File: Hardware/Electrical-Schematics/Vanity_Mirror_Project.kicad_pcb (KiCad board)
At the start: 2 copper layers, 61 x 40.6 mm, 42 parts, among them IC1 SN74LV1T34QDBVRQ1, IC2 FDC1004QDGSRQ1, J1 USB_C_Receptacle_USB2.0_14P, Q1 2N7002, Q2 2N7002, SW1 RST, U1 CH340C, U2 ESP-12F, U3 USBLC6-2SC6, U4 XL1509-3.3

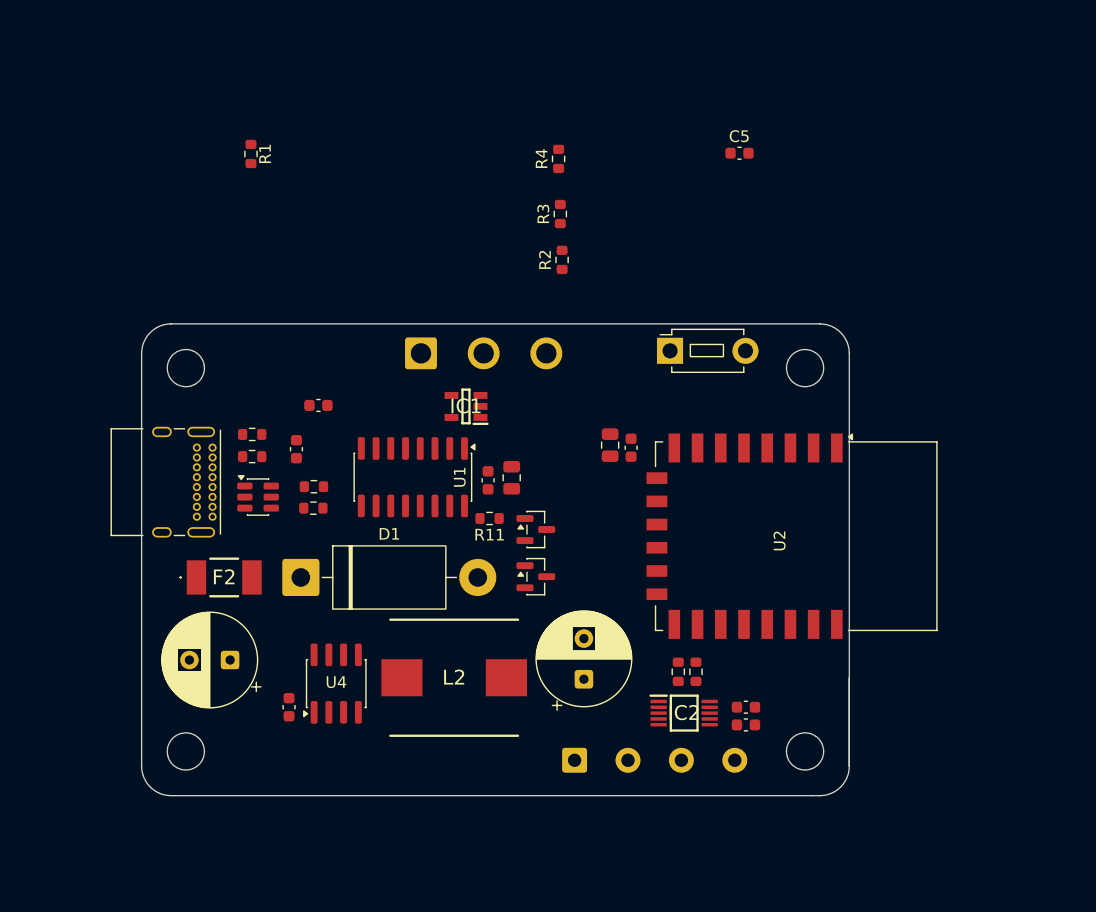
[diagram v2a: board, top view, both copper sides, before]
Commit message: 1st PCB design
Finished the routing of the PCB and added BJTs for auto programming and auto resetting.
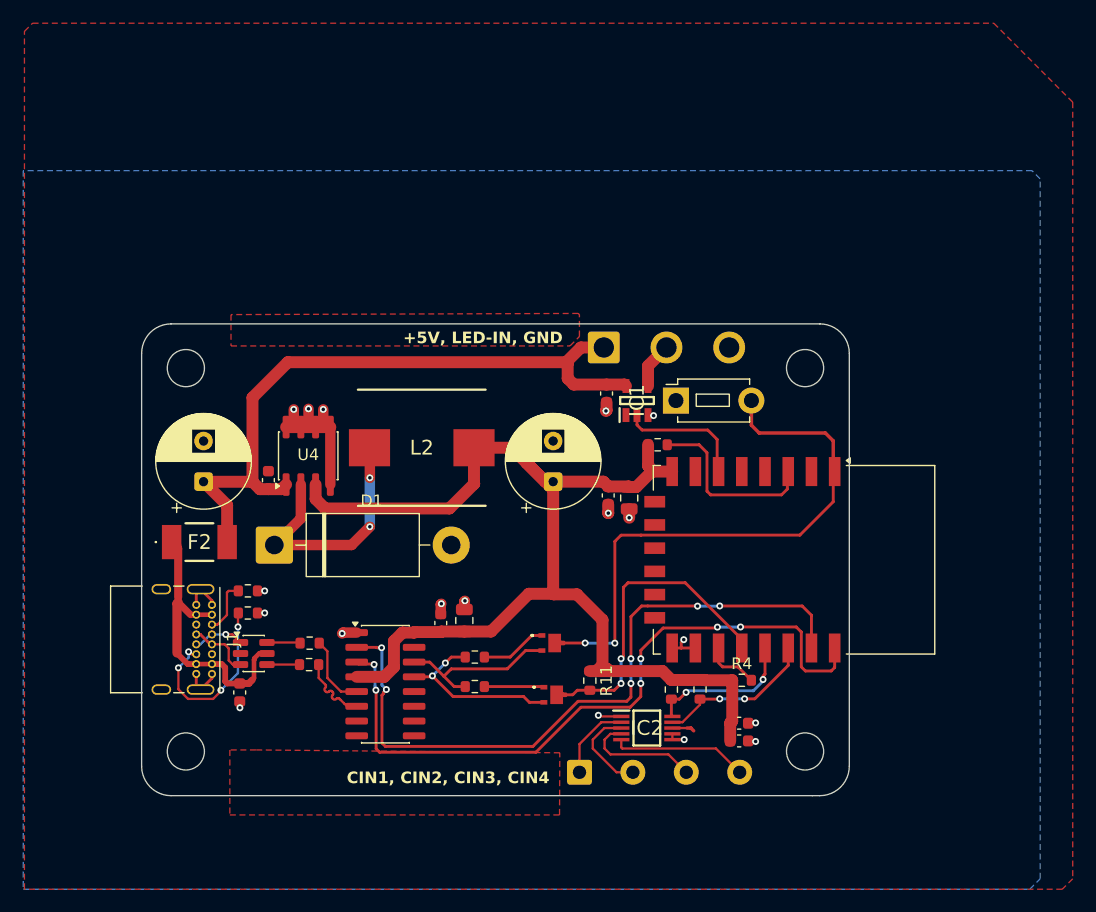
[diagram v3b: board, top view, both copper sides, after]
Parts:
- removed C5: 0.1uF, Capacitor_SMD:C_0603_1608Metric
- Q1, Q2: value 2N7002 -> Q_NPN_BEC; footprint Package_TO_SOT_SMD:SOT-23 -> VanityMirror_FootPrints:PMEG2020EPASX
- R11: value 220 -> 10k
- R2, R3: value 10k -> 12k
- moved R4 47.6 mm to (153.3, 132.3), turned to 0 degrees
- moved R1 43.1 mm to (146.1, 112.0), turned to 180 degrees
- moved R3 41.4 mm to (130.3, 132.8), turned to 180 degrees
- moved R2 35.0 mm to (130.3, 130.3), turned to 180 degrees
- moved C8 24.8 mm to (141.7, 107.6), turned to -90 degrees
- moved C4 21.5 mm to (110.0, 133.3), turned to -90 degrees
- moved L2 20.0 mm to (125.7, 112.3)
- moved U4 19.8 mm to (116.0, 113.0)
- moved C11 19.6 mm to (112.5, 115.1)
- moved U1 18.0 mm to (122.6, 132.6), turned to 0 degrees
- moved C10 17.2 mm to (137.1, 115.2)
- moved R11 16.4 mm to (140.2, 132.3), turned to -90 degrees
- moved LED_Pins1 15.8 mm to (141.4, 103.6)
- moved C12 15.5 mm to (106.9, 115.2), turned to 90 degrees
- moved IC1 14.7 mm to (144.3, 108.2), turned to 90 degrees
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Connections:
- net Net-(U1-UD+) renamed /D+
- net Net-(U1-UD-) renamed /D-
- Q1 pad 1: /~{DTR} -> Net-(Q1-B)
- Q1 pad 2: GND -> Net-(Q1-E)
- Q1 pad 3: Net-(Q1-D) -> /~{RST}
- Q2 pad 1: Net-(Q2-G) -> Net-(Q2-B)
- Q2 pad 2: GND -> Net-(Q2-E)
- Q2 pad 3: Net-(Q2-D) -> /GPIO0
- R11 pad 1: Net-(Q2-G) -> +3.3V
- R11 pad 2: /~{RTS} -> /GPIO0
- R2 pad 1: Net-(Q2-D) -> Net-(Q1-B)
- R2 pad 2: +3.3V -> Net-(Q2-E)
- R3 pad 1: Net-(Q1-D) -> Net-(Q2-B)
- R3 pad 2: +3.3V -> Net-(Q1-E)
- SW1 pad 2: Net-(Q2-D) -> /~{RST}
- U1 pad 13: /~{DTR} -> Net-(Q2-E)
- U1 pad 14: /~{RTS} -> Net-(Q1-E)
- U2 pad 1: Net-(Q2-D) -> /~{RST}
- U2 pad 18: Net-(Q1-D) -> /GPIO0
- U2 pad 19: /SN74_1A -> /SDA
- U2 pad 6: /SDA -> /SN74_1A
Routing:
- net +3.3V: track 0.00 -> 105.2 mm
- net /TX: track 0.00 -> 60.7 mm, vias 0 -> 6
- net /RX: track 0.00 -> 60.1 mm, vias 0 -> 6
- net +5V: track 0.00 -> 59.6 mm
- net /~{RST}: track 0.00 -> 49.2 mm, vias 0 -> 2
- net GND: track 0.00 -> 35.4 mm, vias 0 -> 18
- net /GPIO0: track 0.00 -> 27.4 mm, vias 0 -> 2
- net Net-(U3-VBUS): track 0.00 -> 24.8 mm
- net Net-(D1-K): track 0.00 -> 21.9 mm, vias 0 -> 2
- net Net-(J1-CC2): track 0.00 -> 16.0 mm, vias 0 -> 4
- net Net-(U2-EN): track 0.00 -> 15.8 mm
- net Net-(Q2-E): track 0.00 -> 15.7 mm, vias 0 -> 2
- net Net-(Q1-E): track 0.00 -> 14.6 mm
- net /SCL: track 0.00 -> 13.8 mm, vias 0 -> 2
- net /SDA: track 0.00 -> 13.1 mm, vias 0 -> 2
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- added copper zone on B.Cu, net GND
- added copper zone on F.Cu, net GND
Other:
- outline, holes or cut-outs redrawn
- board text added: "+5V, LED-IN, GND"
- board text added: "CIN1, CIN2, CIN3, CIN4"

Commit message: updating the version
changing laptops so pushing the minor changes made so that the new laptop has the most recent version
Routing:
- net +3.3V: track 105.2 -> 109.1 mm
- net GND: vias 18 -> 22
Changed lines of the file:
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@@
+	)
+	(via
+		(at 146.05 133.223)
+		(size 0.6)
+		(drill 0.3)
+		(layers "F.Cu" "B.Cu")
+		(free yes)
+		(net 1)
 	)
 	(via
@@
 	)
 	(via
+		(at 145.288 133.223)
+		(size 0.6)
+		(drill 0.3)
+		(layers "F.Cu" "B.Cu")
+		(free yes)
+		(net 1)
+	)
+	(via
 		(at 129.4495 125.454)
 		(size 0.6)
@@
 		(drill 0.3)
 		(layers "F.Cu" "B.Cu")
+		(net 1)
+	)
+	(via
+		(at 146.05 133.985)
+		(size 0.6)
+		(drill 0.3)
+		(layers "F.Cu" "B.Cu")
+		(free yes)
+		(net 1)
+	)
+	(via
+		(at 145.288 133.985)
+		(size 0.6)
+		(drill 0.3)
+		(layers "F.Cu" "B.Cu")
+		(free yes)
 		(net 1)
 	)
@@
 	)
 	(segment
+		(start 152.475 134.874)
+		(end 152.475 135.825)
+		(width 1.03)
+		(layer "F.Cu")
+		(net 2)
+	)
+	(segment
 		(start 136.374251 115.190651)
 		(end 137.05 115.190651)
@@
 	)
 	(segment
+		(start 152.221 135.128)
+		(end 152.475 134.874)
+		(width 1.03)
+		(layer "F.Cu")
+		(net 2)
+	)
+	(segment
 		(start 145.63 114.32)
 		(end 147.3 114.32)
@@
 	)
 	(segment
+		(start 148.914 136.414)
+		(end 149.336 136.414)
+		(width 1.03)
+		(layer "F.Cu")
+		(net 2)
+	)
+	(segment
 		(start 137.05 115.190651)
 		(end 141.379651 115.190651)
@@
 	)
 	(segment
+		(start 148.914 136.414)
+		(end 148.586 136.414)
+		(width 0.5)
+		(layer "F.Cu")
+		(net 2)
+	)
+	(segment
 		(start 146.469 131.509)
 		(end 147.234 132.274)
@@
 	)
 	(segment
-		(start 148.914 136.414)
-		(end 149.152 136.652)
-		(width 0.3)
-		(layer "F.Cu")
-		(net 2)
-	)
-	(segment
 		(start 125.1225 128.145)
 		(end 125.075 128.1925)
@@
 	(segment
 		(start 152.475 132.3)
-		(end 152.475 135.825)
+		(end 152.475 134.874)
 		(width 1.03)
 		(layer "F.Cu")
@@
 	)
 	(segment
-		(start 148.586 136.414)
-		(end 148.914 136.414)
-		(width 0.3)
-		(layer "F.Cu")
-		(net 2)
-	)
-	(segment
 		(start 152.3 136)
 		(end 152.3 137.524)
@@
 		(start 141.794 115.605)
 		(end 143.555 115.605)
+		(width 1.03)
+		(layer "F.Cu")
+		(net 2)
+	)
+	(segment
+		(start 150.622 135.128)
+		(end 152.221 135.128)
+		(width 1.03)
+		(layer "F.Cu")
+		(net 2)
+	)
+	(segment
+		(start 149.336 136.414)
+		(end 150.622 135.128)
 		(width 1.03)
 		(layer "F.Cu")
@@
 	)
 	(segment
+		(start 146.875 112.014)
+		(end 149.62 112.014)
+		(width 0.25)
+		(layer "F.Cu")
+		(net 48)
+	)
+	(segment
+		(start 156.591 116.459)
+		(end 157.226 115.824)
+		(width 0.25)
+		(layer "F.Cu")
+		(net 48)
+	)
+	(segment
+		(start 149.62 112.014)
+		(end 150.3 112.694)
+		(width 0.25)
+		(layer "F.Cu")
+		(net 48)
+	)
+	(segment
+		(start 157.226 115.824)
+		(end 157.226 114.37)
+		(width 0.25)
+		(layer "F.Cu")
+		(net 48)
+	)
+	(segment
+		(start 150.3 116.01)
+		(end 150.749 116.459)
+		(width 0.25)
+		(layer "F.Cu")
+		(net 48)
+	)
+	(segment
 		(start 157.226 114.37)
 		(end 157.176 114.32)
@@
 	)
 	(segment
-		(start 150.3 116.01)
-		(end 150.622 116.332)
-		(width 0.25)
-		(layer "F.Cu")
-		(net 48)
-	)
-	(segment
-		(start 156.718 116.332)
-		(end 157.226 115.824)
-		(width 0.25)
-		(layer "F.Cu")
-		(net 48)
-	)
-	(segment
 		(start 150.3 112.694)
 		(end 150.3 116.01)
@@
 	)
 	(segment
-		(start 146.875 112.014)
-		(end 149.62 112.014)
-		(width 0.25)
-		(layer "F.Cu")
-		(net 48)
-	)
-	(segment
-		(start 150.622 116.332)
-		(end 156.718 116.332)
-		(width 0.25)
-		(layer "F.Cu")
-		(net 48)
-	)
-	(segment
-		(start 157.226 115.824)
-		(end 157.226 114.37)
-		(width 0.25)
-		(layer "F.Cu")
-		(net 48)
-	)
-	(segment
-		(start 149.62 112.014)
-		(end 150.3 112.694)
+		(start 150.749 116.459)
+		(end 156.591 116.459)
 		(width 0.25)
 		(layer "F.Cu")
@@
 		(priority 1)
 		(connect_pads
-			(clearance 0.3)
+			(clearance 0.6)
 		)
 		(min_thickness 0.25)
@@
 		(polygon
 			(pts
-				(xy 181.806449 82.5) (xy 181.806449 149.4) (xy 180.906449 150.3) (xy 91.506449 150.3) (xy 91.506449 76.4)
-				(xy 92.206449 75.7) (xy 175.006449 75.7)
+				(xy 187.833 83.312) (xy 187.833 156.337) (xy 187.579 156.591) (xy 88.138 156.591) (xy 88.138 82.677)
+				(xy 187.198 82.677)
 			)
 		)
 		(polygon
 			(pts
-				(xy 109.2 143.9) (xy 120.806449 143.9) (xy 123.006449 143.9) (xy 137.1 143.9) (xy 137.6 143.9) (xy 137.621451 138.547789)
-				(xy 111.44837 138.3) (xy 109.2 138.3)
+				(xy 109.2 139.7) (xy 109.2 142.907978) (xy 110.056022 143.764) (xy 136.652 143.764) (xy 137.16 143.256)
+				(xy 137.16 139.7)
 			)
 		)
 		(polygon
 			(pts
-				(xy 109.3 100.8) (xy 109.3 103.5) (xy 138.5 103.5) (xy 139.312 102.688) (xy 139.312 100.8) (xy 139.212 100.7)
+				(xy 109.22 104.14) (xy 137.16 104.14) (xy 138.684 102.616) (xy 138.684 100.076) (xy 138.176 99.568)
+				(xy 109.22 99.568)
 			)
 		)
@@
 		(polygon
 			(pts
-				(xy 101 134.707978) (xy 108.7 134.707978) (xy 109.2 135.207978) (xy 109.2 142.907978) (xy 108.8 143.307978)
-				(xy 100.9 143.307978) (xy 101 143.207978)
+				(xy 109.2 135.207978) (xy 109.2 142.907978) (xy 108.8 143.307978) (xy 100.9 143.307978) (xy 101 143.207978)
+				(xy 101 134.707978) (xy 108.7 134.707978)
 			)
 		)
